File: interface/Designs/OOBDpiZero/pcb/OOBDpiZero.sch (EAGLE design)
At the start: 101 parts, among them IC3 DS3231, U1 SN65HVD230(SO8), U2 SN65HVD230(SO8), U3 SY6280, U4 SY6280, U5 MP1482, U6 TLV70215

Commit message: add initial version of OOBDpiZero rearrange Eagle library files
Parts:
- removed AM3352-SOM-EVB-PLATFORM: 4XGPH127SMT-02X20(PA-V16X-2X20-LF), OOBDtiger-Connector:OOBD-TIGER-AM3352-SOM---4XGPH127SMT-02X20(PA-V16X-2X20-LF)
- removed C23, C24, C29, C30: 100nF, rcl:C-EUC0603K
- removed C25, C26, C27, C28: 22uF/6.3V, rcl:C-EUC0603
- removed C35, C37, C41, C42: 10µF, SparkFun-Passives:CAP0603-CAP
- removed C36, C43, C44: 0.1µF, SparkFun-Passives:CAP0603-CAP
- removed C38: 0.1nF, SparkFun-Passives:CAP0603-CAP
- removed C57: 1µf, SparkFun-Passives:CAP0603-CAP
- removed C58: NI (47pF), SparkFun-Passives:CAP0603-CAP
- removed C59: 2.2µf, SparkFun-Passives:CAP0603-CAP
- removed L1, L5: FB0805/600R/200mA(201209-601), rcl:L-USL0603
- removed L2, L3, L4: FB0805/600R/2A, rcl:L-USL0603
- removed OOBDPICAN: Bridge to OOBDpiCAN, jumper:JP3Q
- removed R15: 13k/1%, rcl:R-EU_R0603
- removed R16: 6k8k/1%, rcl:R-EU_R0603
- removed R17, R18: 10k, rcl:R-EU_R0603
- removed R19: 10k/1%, rcl:R-EU_R0603
- removed R20, R23: 2.2k/1%, rcl:R-EU_R0603
- removed R21, R24: NI, rcl:R-EU_R0603
- removed R22, R25: 0R, rcl:R-EU_R0603
- removed TLV320AIC1: Audio-Amplifier, TLV320AIC3107:TLV320AIC3107
- removed U4: SY6280, OLIMEX_IC:SY6280
- removed U6: TLV70215, SparkFun-PowerIC:V_REG_LDOSMD
- removed USB_HOST: USB_A_VERTICAL, OLIMEX_CONNECTORS:USB_SHIELD1
- removed USB_OTG: USB-OTG, OLIMEX_CONNECTORS:MINI_USB9
- added U$2: PIZERO_THROUGH_HOLE, pizero:PIZERO_THROUGH_HOLE
- added U$3, U$4: STM32F042CT, micro-stm_v3:STM32F042CT
- U3: value SY6280 -> (none); device OLIMEX_IC:SY6280 -> microbuilder:AUDIOAMP_MAX98357
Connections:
- removed net +5V_OTG_PWR: C23.1, L3.1, USB_OTG.VBUS
- removed net 3V3: AM3352-SOM-EVB-PLATFORM.3.3V@4
- removed net AUD_BCLK: AM3352-SOM-EVB-PLATFORM.P3_14/SPI1_CLK, TLV320AIC1.BCLK
- removed net AUD_DIN: AM3352-SOM-EVB-PLATFORM.P3_16/SPI1_D1(MOSI), TLV320AIC1.DOUT
- removed net AUD_DOUT: AM3352-SOM-EVB-PLATFORM.P3_17/SPI1_CS0, TLV320AIC1.DIN
- removed net AUD_MCLK: AM3352-SOM-EVB-PLATFORM.P3_21/LED3, TLV320AIC1.MCLK
- removed net AUD_WCLK: AM3352-SOM-EVB-PLATFORM.P3_15/SPI1_D0(MISO), TLV320AIC1.WCLK
- removed net DVDD: C37.2, C38.2, C59.2, TLV320AIC1.DVDD, U6.OUT
- removed net N$100: C25.1, C27.1, L3.2, R20.2, U3.OUT
- removed net N$12: C58.2, U6.BP
- removed net N$13: C26.1, C28.1, L4.1, R23.2, U4.OUT
- removed net N$17: R28.1, TLV320AIC1.SPOP
- removed net N$18: R29.1, TLV320AIC1.SPOM
- removed net N$266: L1.2, USB_OTG.GND1, USB_OTG.GND2, USB_OTG.GND3, USB_OTG.GND4
- removed net N$28: C24.1, L4.2, USB_HOST.1
- removed net N$29: L2.2, USB_HOST.5, USB_HOST.6
- removed net N$3: R16.2, U4.ISET
- removed net N$99: R15.2, U3.ISET
- removed net USB0_CE: AM3352-SOM-EVB-PLATFORM.USB0_CE, R21.2
- removed net USB0_DM: AM3352-SOM-EVB-PLATFORM.USB0_DM, USB_OTG.D-
- removed net USB0_DP: AM3352-SOM-EVB-PLATFORM.USB0_DP, USB_OTG.D+
- removed net USB0_DRV: AM3352-SOM-EVB-PLATFORM.USB0-DRV, R22.2
- removed net USB0_EN: R17.2, R21.1, R22.1, U3.EN
- removed net USB0_ID: AM3352-SOM-EVB-PLATFORM.USB0-ID, USB_OTG.ID
- removed net USB0_VBUS: AM3352-SOM-EVB-PLATFORM.USB0-VBUS, R20.1
- removed net USB1_CE: AM3352-SOM-EVB-PLATFORM.USB1_CE, R24.2
- removed net USB1_DM: AM3352-SOM-EVB-PLATFORM.USB1_DM, OOBDPICAN.2, USB_HOST.2
- removed net USB1_DP: AM3352-SOM-EVB-PLATFORM.USB1_DP, OOBDPICAN.4, USB_HOST.3
- removed net USB1_DRV: AM3352-SOM-EVB-PLATFORM.USB1_DRV, R25.2
- removed net USB1_EN: R18.2, R24.1, R25.1, U4.EN
- removed net USB1_ID: AM3352-SOM-EVB-PLATFORM.USB1_ID, R19.2
- removed net USB1_VBUS: AM3352-SOM-EVB-PLATFORM.USB1-VBUS, R23.1
- net +3V3: no longer AM3352-SOM-EVB-PLATFORM.3.3V@3, C35.2, C36.2, C41.1, C42.1, C43.1, C44.1, C57.2, TLV320AIC1.AVDD_ADC, TLV320AIC1.AVDD_DAC, TLV320AIC1.DRVDD_0, TLV320AIC1.DRVDD_1, TLV320AIC1.IOVDD, U6.EN, U6.IN
- net +5V: no longer AM3352-SOM-EVB-PLATFORM.5.0V@3, AM3352-SOM-EVB-PLATFORM.5.0V@4, C29.1, C30.1, OOBDPICAN.1, TLV320AIC1.SPVDD, U3.IN, U4.IN
- net AGND: no longer L5.2, TLV320AIC1.AVSS_ADC, TLV320AIC1.AVSS_DAC, TLV320AIC1.SWINM, TLV320AIC1.SWINP
- net DCAN0_RX: no longer AM3352-SOM-EVB-PLATFORM.P0_13/I2C2_SCL
- net DCAN0_TX: no longer AM3352-SOM-EVB-PLATFORM.P0_12/I2C2_SDA
- net DCAN1_RX: no longer AM3352-SOM-EVB-PLATFORM.P1_9/UART4_TXD
- net DCAN1_TX: no longer AM3352-SOM-EVB-PLATFORM.P1_8/UART4_RXD
- net EXT_WAKEUP: no longer AM3352-SOM-EVB-PLATFORM.EXT_WAKEUP
- net GND: no longer AM3352-SOM-EVB-PLATFORM.GND@5, AM3352-SOM-EVB-PLATFORM.GND@6, AM3352-SOM-EVB-PLATFORM.GND@7, AM3352-SOM-EVB-PLATFORM.GND@8, AM3352-SOM-EVB-PLATFORM.GNDA, C23.2, C24.2, C25.2, C26.2, C27.2, C28.2, C29.2, C30.2, C35.1, C36.1, C37.1, C38.1, C41.2, C42.2, C43.2, C44.2, C57.1, C58.1, C59.1, L1.1, L2.1, L5.1, OOBDPICAN.5, R15.1, R16.1, R17.1, R18.1, R19.1, TLV320AIC1.DRVSS, TLV320AIC1.DVSS, TLV320AIC1.SPVSS, U3.GND, U4.GND, U6.GND, USB_HOST.4, USB_OTG.GND
- net HS-CAN_RS: no longer AM3352-SOM-EVB-PLATFORM.P3_8/EMU1
- net I2C0-SCL: no longer AM3352-SOM-EVB-PLATFORM.P3_6/I2C0-SCL, TLV320AIC1.SCL
- net I2C0-SDA: no longer AM3352-SOM-EVB-PLATFORM.P3_5/I2C0-SDA, TLV320AIC1.SDA
- net LED1: no longer AM3352-SOM-EVB-PLATFORM.P3_18/LED1
- net LED2: no longer AM3352-SOM-EVB-PLATFORM.P3_20/LED2
- net MS-CAN_RS: no longer AM3352-SOM-EVB-PLATFORM.P3_7/EMU0
- net N$14: no longer TLV320AIC1.RIGHT_LOP
- net N$19: no longer TLV320AIC1.LEFT_LOP
- net SYS_RESETN: no longer AM3352-SOM-EVB-PLATFORM.SYS_RESETN@3, TLV320AIC1.RESETN
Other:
- note added: "Pi Zero GPIO"
- note added: "Title: Connector for Pi Zero GPIO"
- note removed: "1000mA"
- note removed: "523mA"
- note removed: "AM3352-SOM-EVB Interconnectors"
- note removed: "Iset = 523mA"
- note removed: "Iset = 6800/Rs"
- note removed: "OOBDpiCAN connector"
- note removed: "Power Supply 1V8, Audio-Interface"
- note removed: "Rs"
- note removed: "Title: Connector for AM3352SOM"
- note removed: "Title: USB-Interfaces (OTG / HOST)"
- note removed: "USB0-OTG"
- note removed: "USB1-HOST"

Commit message: modify OOBpiZero due to schematic review
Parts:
- removed C39: 22µF, SparkFun-Passives:CAP0603-CAP
- removed C40: 0.1µF, SparkFun-Passives:CAP0603-CAP
- removed C49: 100nF, rcl:C-EUC0603
- removed LED1: LED/Yellow/0603, DOUBLE-SIDE:LEDLED_0603
- removed LED2: LED/Red/0603, DOUBLE-SIDE:LEDLED_0603
- removed OOBD2-CONNECTOR: In-Car Diagnostic, pinhead:PINHD-2X5/90
- removed R30, R38, R40: 2.2k/1%, rcl:R-EU_R0603
- removed R31: NI, rcl:R-EU_R0603
- removed R34: 49.9R/1%, rcl:R-EU_R0603
- removed U$4: STM32F042CT, micro-stm_v3:STM32F042CT
- removed WAKE-UP: Open, SparkFun:JUMPER-2PTH_LOCK
- added C1, C24, C25, C30: 100nF, rcl:C-EUC0603K
- added C10, C12, C13, C15, C18, C19, C2, C20, C5, C57, C59, C6, C7, C8, C9: 100nF, resistor:C-EUC0603
- added C16, C17: 33pF, resistor:C-EUC0603
- added C21: 1uF, resistor:C-EUC0603
- added C23: 100nF, rcl:C-EUC0603
- added C26, C27, C28, C29: 22uF/6.3V, rcl:C-EUC0603
- added C4: 10uF, rcl:C-EUC0805K
- added C58, C60: 22uF/6.3V, rcl:CPOL-EUSMCA
- added GPIO: PIZERO_THROUGH_HOLE, pizero:PIZERO_THROUGH_HOLE
- added IC11: EEPROM24, FLYFISH:EEPROM24
- added JP2, JP3: (no value), jumper:JP4E
- added JP4: (no value), jumper:JP2E
- added L1: 2508056017Y2, rcl:L-EUL0805
- added L3, L4, L5, L7: FB0805/600R/2A, rcl:L-USL0603
- added LED3, LED6: gr, DOUBLE-SIDE:LEDLED_0603
- added LED4, LED7: yel, DOUBLE-SIDE:LEDLED_0603
- added LED5, LED8: red, DOUBLE-SIDE:LEDLED_0603
- added Q2: 12MHz, crystal:CRYSTALSM49
- added R1, R25, R41, R6: 10k, rcl:R-EU_R0603
- added R13, R14, R15, R17, R18, R19, R20, R8: 330R, rcl:R-EU_R0603
- added R16, R7: 60R, resistor:R-EU_R0603
- added R21, R22: 10k, resistor:R-EU_R0603
- added R23: NA(47k), resistor:R-EU_R0603
- added R24: 6k8k/1%, rcl:R-EU_R0603
- added R42: 2.2k/1%, rcl:R-EU_R0603
- added R43, R44: NI, rcl:R-EU_R0603
- added R52, R53: NI, resistor:R-EU_R0603
- added SJ1: SOLDERJUMPERTRACE, SparkFun:SOLDERJUMPERTRACE
- added U$5: GL850G-31, pimoroni:GL850G-31
- added U4: SY6280, OLIMEX_IC:SY6280
- added USB_HOST1, USB_HOST2: USB_A_VERTICAL, OLIMEX_CONNECTORS:USB_SHIELD1
- C45, C46: value NI (0,01µF) -> 220pF; device SparkFun-Passives:CAP0603-CAP -> rcl:C-EUC0603K
- JP1: value Audio-Out -> (none); device jumper:JP3Q -> jumper:JP1Q
- R26: value 10K -> 1M
- R27: value 10K -> 680R; MANEX 110-0002014 -> (none)
- R28, R29: value 0R -> 10k; device resistor:R-EU_R0805 -> rcl:R-EU_R0603
- R33: device rcl:R-EU_R0603 -> resistor:R-EU_R0603
- U$2: value PIZERO_THROUGH_HOLE -> STM32F042CT; device pizero:PIZERO_THROUGH_HOLE -> micro-stm_v3:STM32F042CT
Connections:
- removed net AGND: C45.1, C46.1, JP1.5
- removed net DCAN0_RX: U2.RXD
- removed net DCAN0_TX: U2.TXD
- removed net DCAN1_RX: U1.RXD
- removed net DCAN1_TX: U1.TXD
- removed net EXT_WAKEUP: R34.1
- removed net I2C0-SCL: IC3.SCL, R26.1
- removed net I2C0-SDA: IC3.SDA, R27.1
- removed net LED1: R38.1
- removed net LED2: R40.1
- removed net N$1: LED2.A, R40.2
- removed net N$231: LED1.A, R38.2
- removed net N$43: R30.1, WAKE-UP.1
- removed net N$44: C49.1, R31.1, R34.2, WAKE-UP.2
- removed net SYS_RESETN: IC3.!RST
- new net AUD_BCLK: GPIO.18, U3.BCLK
- new net AUD_DIN: GPIO.21, U3.DIN
- new net AUD_LRCLK: GPIO.19, U3.LRCLK
- new net AUD_SD_MODE: GPIO.29, R26.1, U3.!SD_MODE
- new net HS-CAN_RXD: U$3.PB8, U1.RXD
- new net HS-CAN_TXD: U$3.PB9, U1.TXD
- new net ID_SC: GPIO.28, IC11.SCL, R29.2
- new net ID_SD: GPIO.27, IC11.SDA, R25.2
- new net MS-CAN_RXD: U$2.PB8, U2.RXD
- new net MS-CAN_TXD: U$2.PB9, U2.TXD
- new net N$12: C46.2, JP1.1, U3.OUTP
- new net N$13: R8.2, U$3.PA0
- new net N$17: LED5.C, R14.1
- new net N$18: LED4.C, R13.1
- new net N$20: C9.2, R15.2, U$3.NRST
- new net N$21: R16.1, U$2.PF11-BOOT0
- new net N$22: R17.2, U$2.PA0
- new net N$23: R18.2, U$2.PA1
- new net N$24: R19.2, U$2.PA2
- new net N$25: LED8.C, R19.1
- new net N$26: LED7.C, R18.1
- new net N$28: C15.2, R20.2, U$2.NRST
- new net N$29: C17.1, Q2.2, U$5.X2
- new net N$3: C45.2, JP1.2, U3.OUTN
- new net N$31: C16.1, Q2.1, U$5.X1
- new net N$33: C57.1, C58.+, L1.2, R21.2, R33.2, U$5.DVDD, U$5.V33
- new net N$34: R33.1, U$5.PGANG
- new net N$35: R21.1, U$5.PSELF
- new net N$36: C21.1, R22.2, R23.2, U$5.RESET#
- new net N$37: R52.2, R53.1, U3.GAIN
- new net N$39: C18.1, C19.1, C20.1, L1.1, U$5.AVDD, U$5.AVDD2, U$5.AVDD3
- new net N$40: R27.2, U$5.RREF
- new net N$41: C24.1, L4.2, USB_HOST1.1
- new net N$42: L3.2, USB_HOST1.5, USB_HOST1.6
- new net N$45: R24.2, U4.ISET
- new net N$46: IC11.WP, R28.2, SJ1.2
- new net N$47: C26.1, C27.1, C28.1, C29.1, L4.1, L5.1, R42.2, U4.OUT
- new net N$48: C25.1, L5.2, USB_HOST2.1
- new net N$49: L7.2, USB_HOST2.5, USB_HOST2.6
- new net PP22: U$5.DP0
- new net PP23: U$5.DM0
- new net SCL: GPIO.5, IC3.SCL, R1.2
- new net SDA: GPIO.3, IC3.SDA, R6.2
- new net SWCLK: JP2.3, JP3.3, U$2.PA14, U$3.PA14
- new net SWDIO: JP2.2, JP3.2, U$2.PA13, U$3.PA13
- new net UART0_RXD: GPIO.10, JP4.2
- new net UART0_TXD: GPIO.8, JP4.1
- new net USB0_DM: U$3.PA11, U$5.DM1
- new net USB0_DP: U$3.PA12, U$5.DP1
- new net USB1_DM: U$2.PA11, U$5.DM2
- new net USB1_DP: U$2.PA12, U$5.DP2
- new net USB1_EN: R41.2, R43.1, R44.1, U4.EN
- new net USB2_DM: U$5.DM3, USB_HOST1.2
- new net USB2_DP: U$5.DP3, USB_HOST1.3
- new net USB3_DM: U$5.DM4, USB_HOST2.2
- new net USB3_DP: U$5.DP4, USB_HOST2.3
- new net USB_CE: GPIO.31, R43.2
- new net USB_VBUS: GPIO.32, R42.1
- net +12V: no longer OOBD2-CONNECTOR.10
- net +3V3: now also C10.2, C12.2, C13.2, C2.2, C5.2, C6.2, C7.2, C8.2, GPIO.1, GPIO.17, JP2.1, JP3.1, LED3.A, LED4.A, LED5.A, LED6.A, LED7.A, LED8.A, R1.1, R15.1, R20.1, R44.2, R6.1, U$2.VBAT, U$2.VDD1, U$2.VDD2, U$2.VDDA, U$2.VDDIO2, U$3.VBAT, U$3.VDD1, U$3.VDD2, U$3.VDDA, U$3.VDDIO2; no longer R26.2, R27.2, R30.2, R33.2
- net +5V: now also C1.1, C23.2, C30.1, C4.1, C59.1, C60.+, GPIO.2, GPIO.4, IC11.VCC, R22.1, R25.1, R26.2, R28.1, R29.1, R53.2, U$5.V5, U3.VDD, U4.IN; no longer C39.2, C40.2
- net GND: now also C1.2, C10.1, C12.1, C13.1, C15.1, C16.2, C17.2, C18.2, C19.2, C2.1, C20.2, C21.2, C23.1, C24.2, C25.2, C26.2, C27.2, C28.2, C29.2, C30.2, C4.2, C45.1, C46.1, C5.1, C57.2, C58.-, C59.2, C6.1, C60.-, C7.1, C8.1, C9.1, GPIO.14, GPIO.20, GPIO.25, GPIO.30, GPIO.34, GPIO.39, GPIO.6, GPIO.9, IC11.A0, IC11.A1, IC11.A2, IC11.GND, JP2.4, JP3.4, JP4.3, L3.1, L7.1, R16.2, R23.1, R24.1, R27.1, R41.1, R52.1, R7.2, SJ1.1, U$2.VSS1, U$2.VSS2, U$2.VSS3, U$2.VSSA, U$3.VSS1, U$3.VSS2, U$3.VSS3, U$3.VSSA, U$5.GND, U$5.TEST/SCL, U3.GND, U4.GND, USB_HOST1.4, USB_HOST2.4; no longer C39.1, C40.1, C49.2, JP1.6, LED1.C, LED2.C, OOBD2-CONNECTOR.3, R31.2
- net HS-CAN_H: no longer OOBD2-CONNECTOR.7
- net HS-CAN_L: no longer OOBD2-CONNECTOR.6
- net HS-CAN_RS: now also GPIO.35
- net MS-CAN_H: no longer OOBD2-CONNECTOR.1
- net MS-CAN_L: no longer OOBD2-CONNECTOR.2
- net MS-CAN_RS: now also GPIO.36
- net N$14: now also R13.2, U$3.PA1; no longer JP1.1
- net N$15: now also R7.1, U$3.PF11-BOOT0; no longer C45.2, JP1.4, R29.2
- net N$16: now also R14.2, U$3.PA2; no longer C46.2, JP1.2, R28.2
- net N$19: now also LED3.C, R8.1; no longer JP1.3
- net N$27: now also LED6.C, R17.1; no longer IC3.!INT, R33.1
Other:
- note added: "1000mA"
- note added: "4-Port USB-HUB"
- note added: "Author: M. Luxen"
- note added: "EEPROM"
- note added: "MS-CAN Interface (optional)"
- note added: "Project: OOBDpiZero"
- note added: "Title: 4-Port USB-HUB USB2 / USB3 Interface"
- note added: "Title: Audio Power Supply RTC Pi-Zero GPIO"
- note added: "Title: CAN Interfaces"
- note added: "USB2-HOST (extern)"
- note added: "USB3-HOST (intern)"
- note removed: "Author: W. Sauer, M. Luxen"
- note removed: "Button"
- note removed: "LEDs"
- note removed: "Line-Out"
- note removed: "MS-CAN Interface (default)"
- note removed: "OBD2 Internal-Connector"
- note removed: "OBD2-Power supply"
- note removed: "Project: OOBD-Tiger"
- note removed: "Title: Audio Interface"
- note removed: "Title: Connector for Pi Zero GPIO"
- note removed: "Title: HS-CAN Interface"
- note removed: "Title: Power Supply"

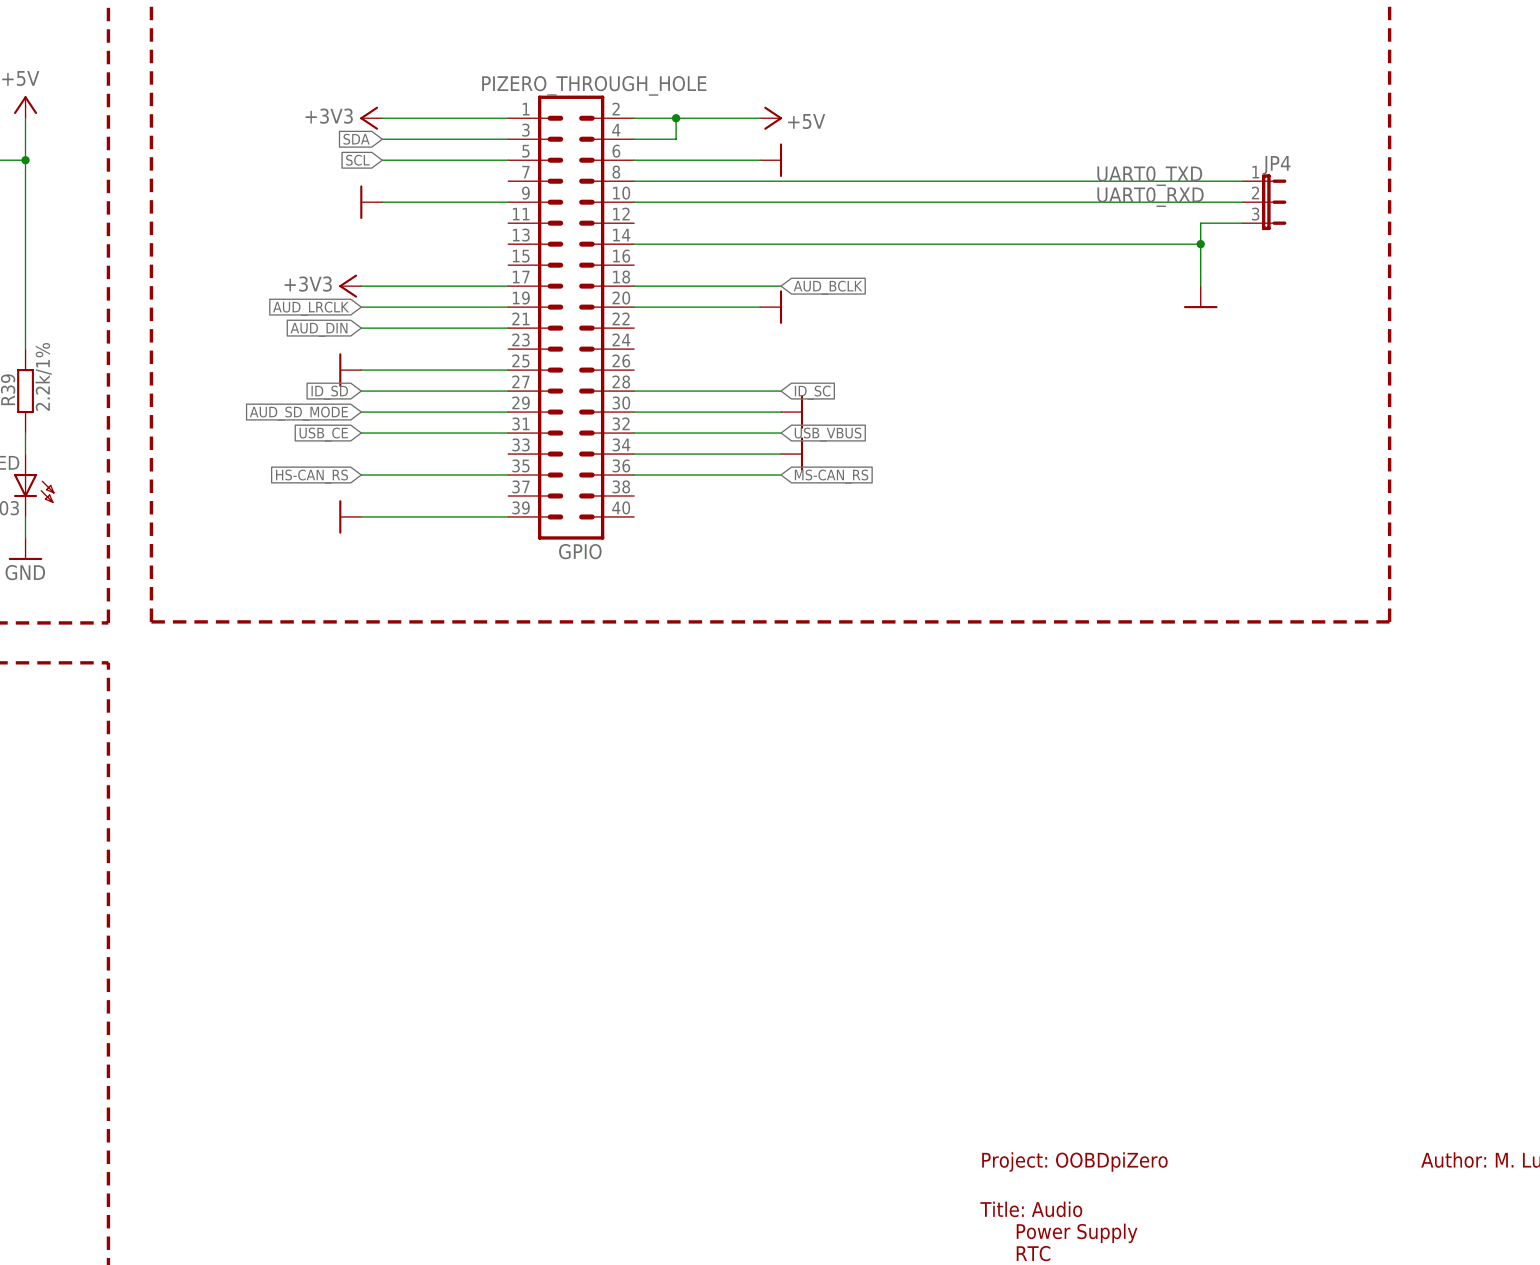
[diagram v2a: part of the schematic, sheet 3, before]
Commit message: - replace internal USB-A with micro-USB connector - connect "old" internal USB interface to micro-USB connector to either use as 5V power supply or USB-HUB input as external AddOn extension - add missing 3V3 LDO (optional) for use without Pi Zero (W)
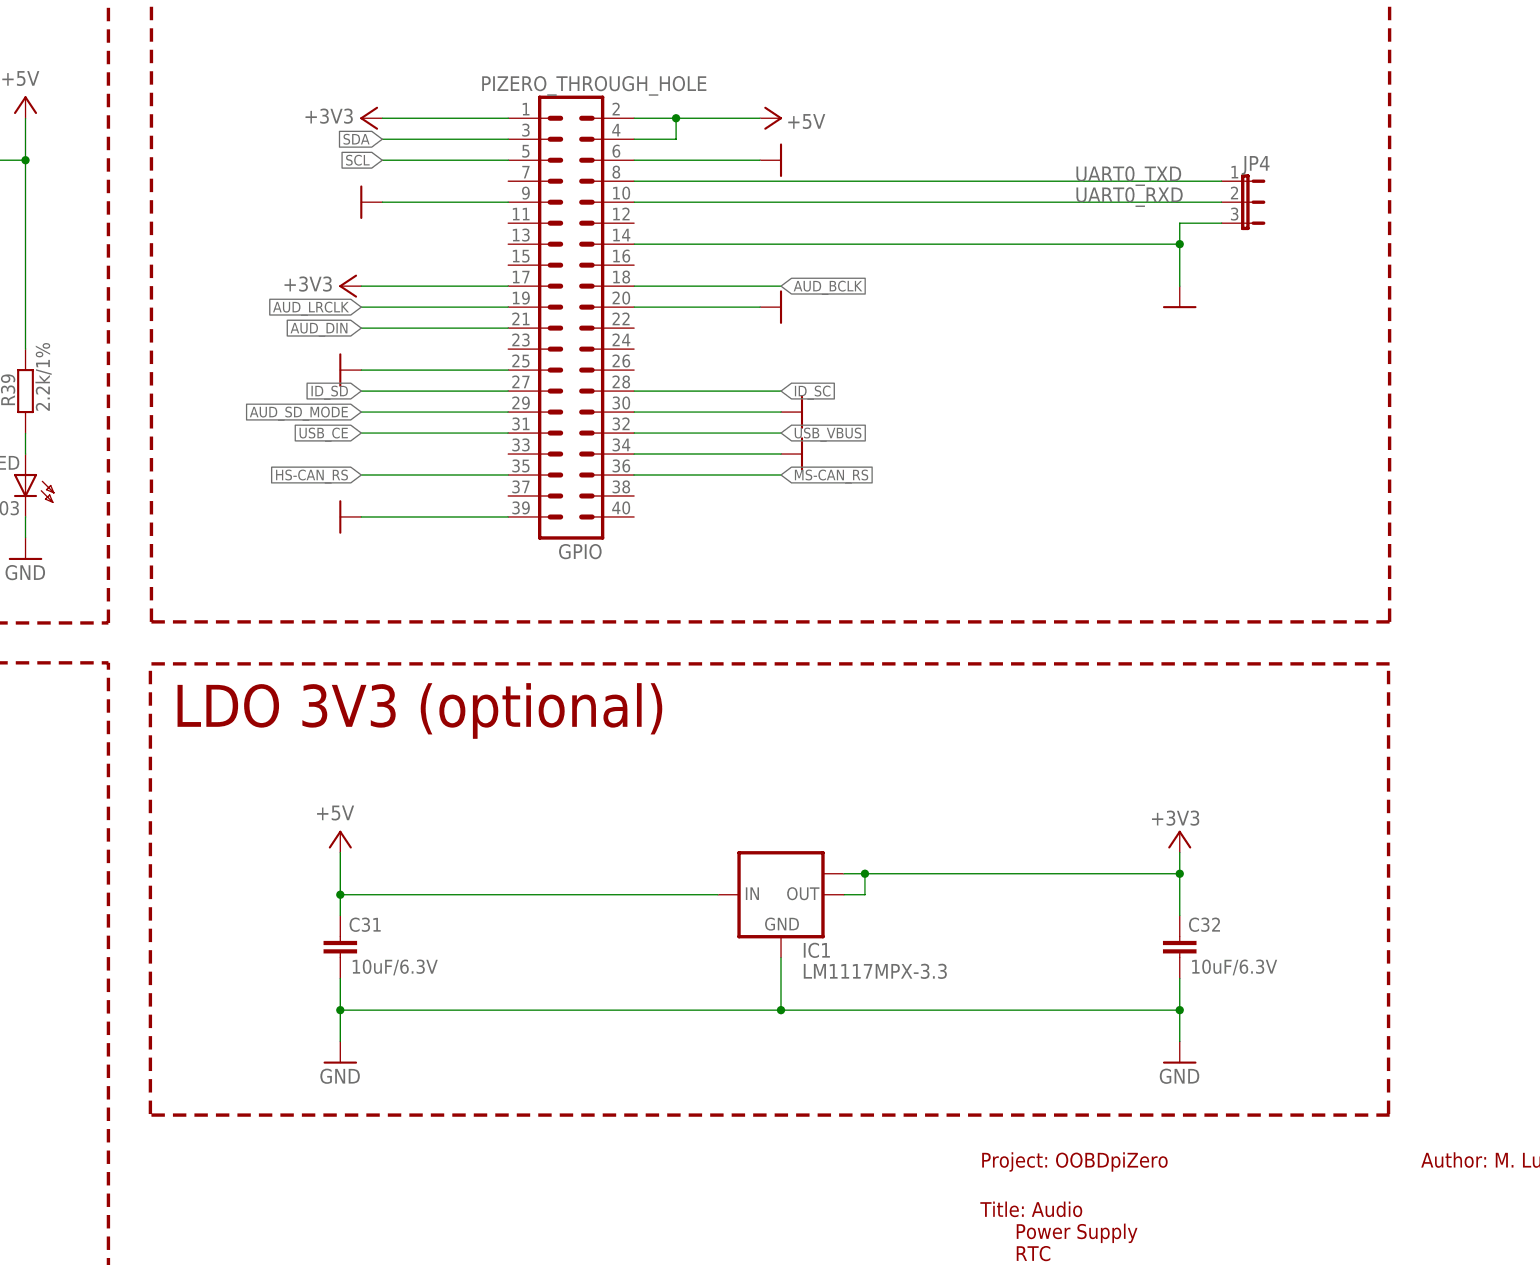
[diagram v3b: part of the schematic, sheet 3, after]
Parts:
- added C31, C32: 10uF/6.3V, rcl:C-EUC0603
- added IC1: LM1117MPX-3.3, lm1117:LM1117MPX-3.3
- added R30, R31: NI(0R), resistor:R-EU_R0603
- added R34: NI(0R), resistor:R-EU_R0805
- USB_HOST2: device OLIMEX_CONNECTORS:USB_SHIELD1 -> con-molex-usb:MICRO-USB-RECEPTACLE47589-0001
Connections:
- new net N$1: C27.1, C29.1, L5.1, R34.1
- net +3V3: now also C32.1, IC1.OUT, IC1.OUT1
- net +5V: now also C31.1, IC1.IN, R34.2
- net GND: now also C31.2, C32.2, IC1.GND
- net N$47: no longer C27.1, C29.1, L5.1
- net N$49: no longer USB_HOST2.6
- net PP22: now also R31.2
- net PP23: now also R30.2
- net USB3_DM: now also R30.1
- net USB3_DP: now also R31.1
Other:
- note added: "LDO 3V3 (optional)"
- moved on the sheet: JP4
